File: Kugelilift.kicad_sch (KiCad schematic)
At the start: 16 parts, among them J2 TTL, J4 Stepper, SW1 RESET, SW2 MODE, SW3 SW_Push, SW4 SW_DIP_x04, U1 magnetic-charger, U2 TCRT5000, U3 ULN2003A, U5 UA78M33_TO252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

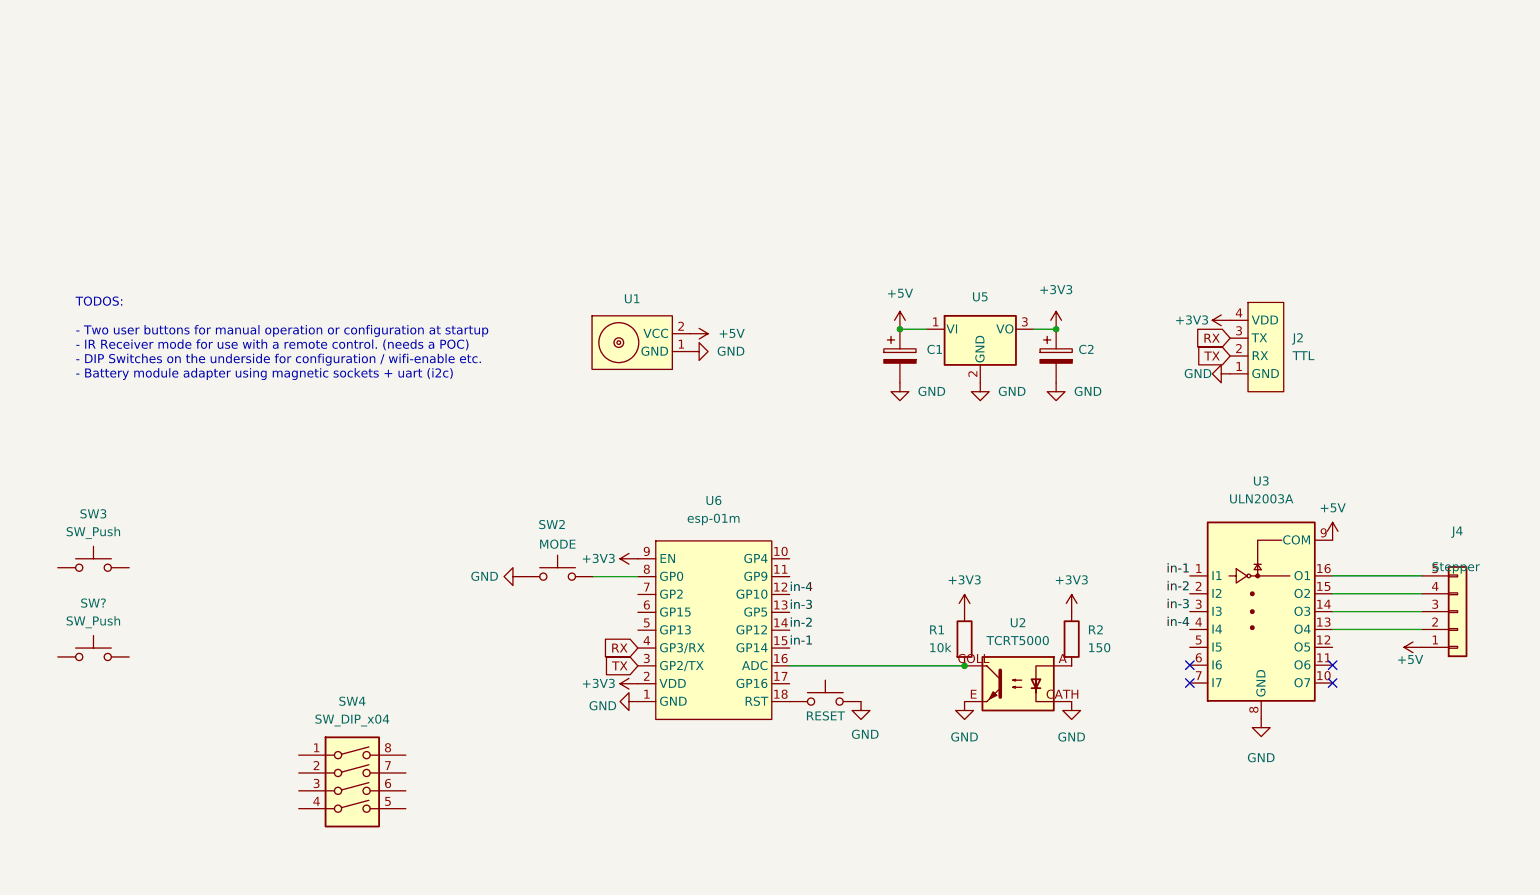
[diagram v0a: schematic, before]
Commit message: Laid out pushbuttons and dip switches
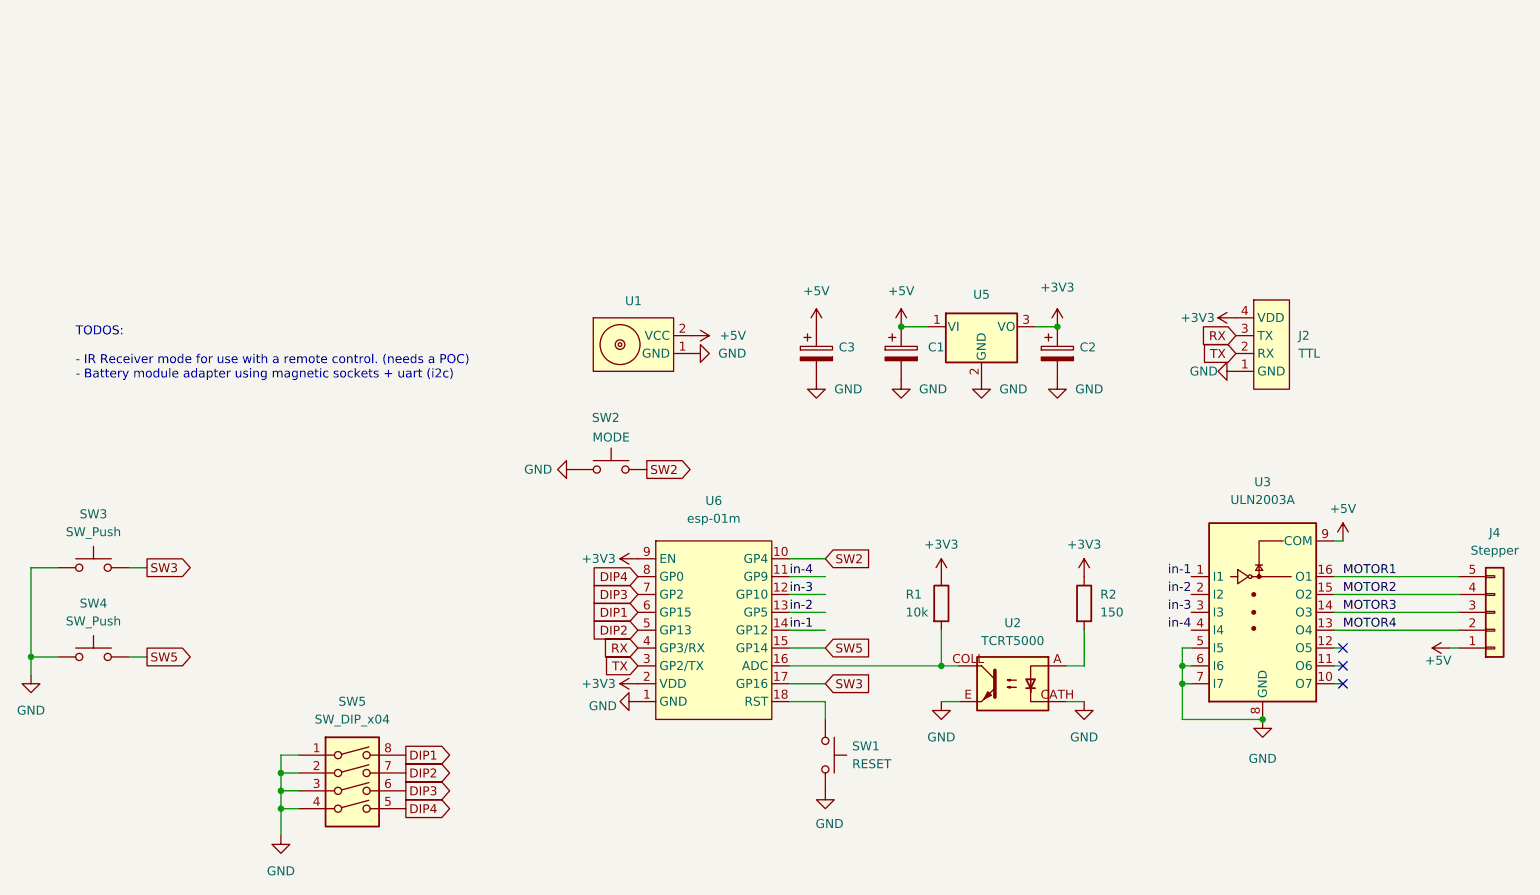
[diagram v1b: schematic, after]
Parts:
- added C3: C_Polarized, Capacitor_THT:CP_Radial_D6.3mm_P2.50mm, symbol Device:C_Polarized
- U3: footprint Package_SO:SOP-16_4.55x10.3mm_P1.27mm -> Package_SO:SOIC-16_3.9x9.9mm_P1.27mm
- gave numbers to parts that had none: 1
- renumbered SW4 to SW5
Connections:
- net +5V: now also C3.1
- net GND: now also SW3.1, SW4.1, SW5.1, SW5.2, SW5.3, SW5.4, U3.5 (I5), U3.6 (I6), U3.7 (I7), C3.2
- net in-1: now also U6.14 (GP12); no longer U6.15 (GP14)
- net in-2: now also U6.13 (GP5); no longer U6.14 (GP12)
- net in-3: now also U6.12 (GP10); no longer U6.13 (GP5)
- net in-4: now also U6.11 (GP9); no longer U6.12 (GP10)
- net MOTOR4: now reaches J4.2 (Pin_2), U3.13 (O4)
- net MOTOR3: now reaches J4.3 (Pin_3), U3.14 (O3)
- net MOTOR2: now reaches J4.4 (Pin_4), U3.15 (O2)
- net MOTOR1: now reaches J4.5 (Pin_5), U3.16 (O1)
- net DIP4: now reaches U6.8 (GP0)
- net DIP4: now also SW5.5; no longer SW2.1
- net SW2: now reaches U6.10 (GP4)
- net SW2: now also SW2.1
- net SW3: now reaches U6.17 (GP16)
- net SW3: now also SW3.2
- net DIP2: now reaches U6.5 (GP13)
- net DIP2: now also SW5.7
- net DIP1: now reaches U6.6 (GP15)
- net DIP1: now also SW5.8
- net DIP3: now reaches U6.7 (GP2)
- net DIP3: now also SW5.6
- net SW5: now reaches SW4.2
- net SW5: now also U6.15 (GP14)
- no-connect marks 4 -> 3
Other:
- note added: "TODOS: - IR Receiver mode for use with a remote control. (needs a POC) - Battery module adapter using magnetic sockets + uart (i2c)"
- note removed: "TODOS: - Two user buttons for manual operation or configuration at startup - IR Receiver mode for use with a remote control. (needs a POC) - DIP Switches on the underside for configuration / wifi-enable etc. - Battery module adapter using magnetic sockets + uart (i2c)"
- moved on the sheet: J2, J4, R1, R2, SW2, U2

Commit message: Update to "hard" pushbuttons, rearrange components.
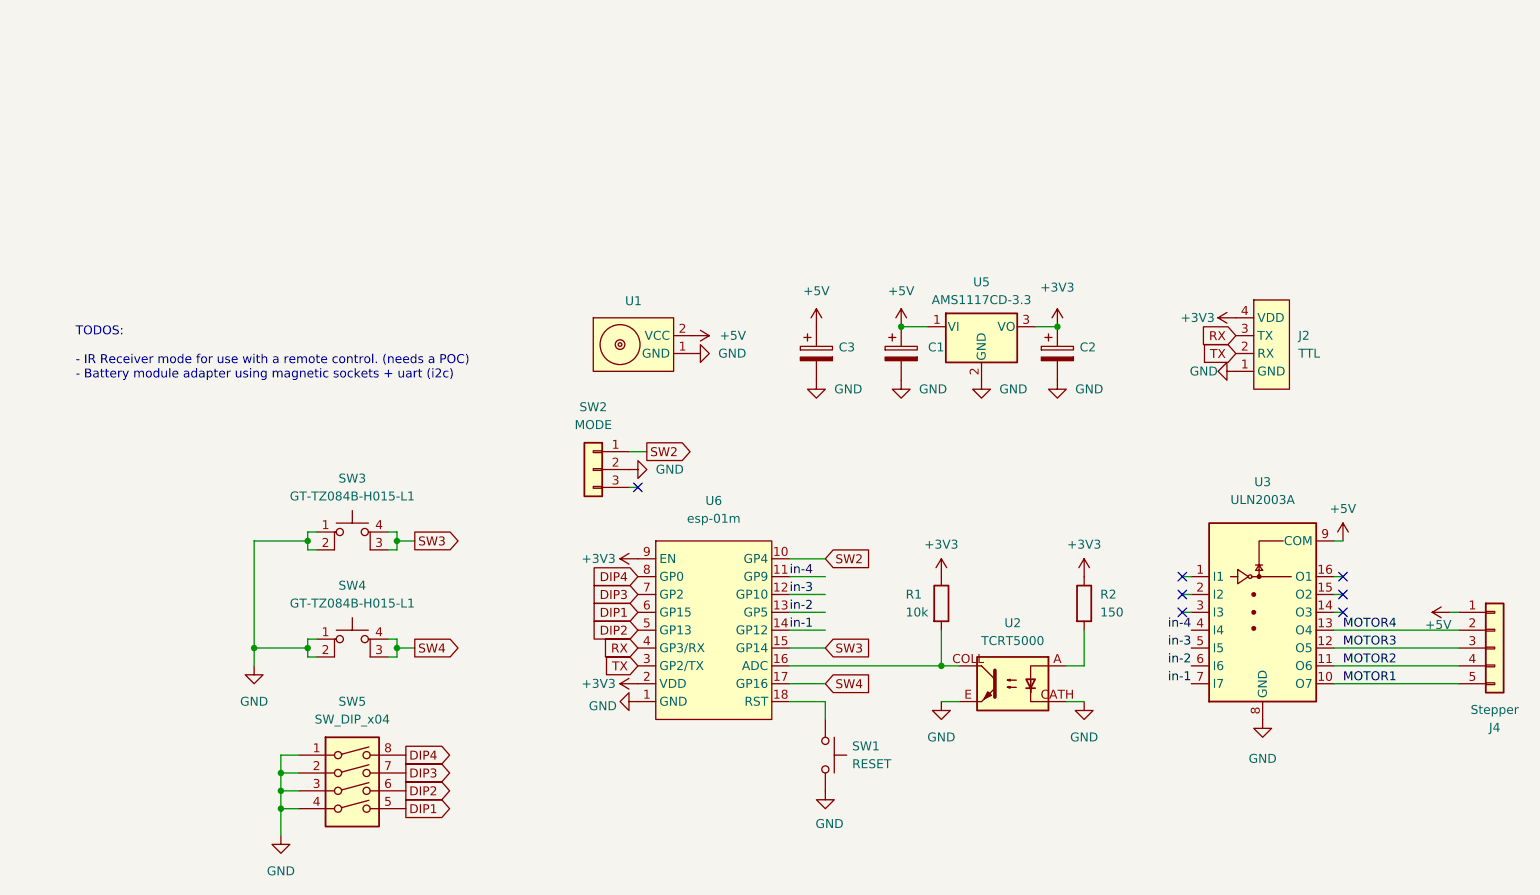
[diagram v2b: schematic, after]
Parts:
- removed SW3, SW4: SW_Push, Button_Switch_SMD:SW_Push_1P1T_NO_CK_KMR2, symbol Switch:SW_Push
- added SW3, SW4: GT-TZ084B-H015-L1, jlc_footprints:SW-SMD_4P-L5.2-W5.2-P3.70-LS6.4, symbol jlc_symbols:GT-TZ084B-H015-L1
- SW2: symbol Switch:SW_Push -> Connector_Generic:Conn_01x03
- U5: value UA78M33_TO252 -> AMS1117CD-3.3
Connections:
- net SW5 is gone; now on net SW3: U6.15 (GP14)
- net DIP1: now also SW5.5; no longer SW5.8
- net DIP2: now also SW5.6; no longer SW5.7
- net DIP3: now also SW5.7; no longer SW5.6
- net DIP4: now also SW5.8; no longer SW5.5
- net GND: now also SW3.1, SW3.2, SW4.1, SW4.2; no longer U3.5 (I5), U3.6 (I6), U3.7 (I7)
- net MOTOR1: now also U3.10 (O7); no longer U3.16 (O1)
- net MOTOR2: now also U3.11 (O6); no longer U3.15 (O2)
- net MOTOR3: now also U3.12 (O5); no longer U3.14 (O3)
- net SW3: now also SW3.3, SW3.4; no longer U6.17 (GP16)
- net in-1: now also U3.7 (I7); no longer U3.1 (I1)
- net in-2: now also U3.6 (I6); no longer U3.2 (I2)
- net in-3: now also U3.5 (I5); no longer U3.3 (I3)
- new net SW4: SW4.3, SW4.4, U6.17 (GP16)
- no-connect marks 3 -> 7
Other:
- moved on the sheet: J4

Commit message: Rearrange components.
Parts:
- added SW32: GT-TZ084B-H015-L1, jlc_footprints:SW-SMD_4P-L5.2-W5.2-P3.70-LS6.4, symbol jlc_symbols:GT-TZ084B-H015-L1
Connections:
- net GND: now also SW32.1, SW32.2
- net MOTOR1: now also U3.13 (O4); no longer U3.10 (O7)
- net MOTOR2: now also U3.14 (O3); no longer U3.11 (O6)
- net MOTOR3: now also U3.15 (O2); no longer U3.12 (O5)
- net MOTOR4: now also U3.16 (O1); no longer U3.13 (O4)
- net SW3: now also SW32.3, SW32.4
- net SW4: no longer SW4.4
- net in-1: now also U3.4 (I4); no longer U3.7 (I7)
- net in-2: now also U3.3 (I3); no longer U3.6 (I6)
- net in-3: now also U3.2 (I2); no longer U3.5 (I5)
- net in-4: now also U3.1 (I1); no longer U3.4 (I4)
- no-connect marks 7 -> 8
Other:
- moved on the sheet: J4, SW3

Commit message: Use the LED footprint.
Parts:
- added U4: SK6812MINI-E_C5149201, jlc_footprints:LED-SMD_L3.2-W2.8-LS5.9_SK6812MINI-E BACK, symbol jlc_symbols:SK6812MINI-E_C5149201
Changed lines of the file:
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@@
+	)
+	(symbol
+		(lib_id "jlc_symbols:SK6812MINI-E_C5149201")
+		(at 73.66 52.07 0)
+		(unit 1)
+		(exclude_from_sim no)
+		(in_bom yes)
+		(on_board yes)
+		(dnp no)
+		(fields_autoplaced yes)
+		(property "Reference" "U4"
+			(at 73.66 43.18 0)
+			(effects
+				(font
+					(size 1.27 1.27)
+				)
+			)
+		)
+		(property "Value" "SK6812MINI-E_C5149201"
+			(at 73.66 45.72 0)
+			(effects
+				(font
+					(size 1.27 1.27)
+				)
+			)
+		)
+		(property "Footprint" "jlc_footprints:LED-SMD_L3.2-W2.8-LS5.9_SK6812MINI-E BACK"
+			(at 73.66 62.23 0)
+			(effects
+				(font
+					(size 1.27 1.27)
+					(italic yes)
+				)
+				(hide yes)
+			)
+		)
+		(property "Datasheet" "https://atta.szlcsc.com/upload/public/pdf/source/20241205/F2A5A00C3A41F444A29929735E36DD04.pdf"
+			(at 71.374 51.943 0)
+			(effects
+				(font
+					(size 1.27 1.27)
+				)
+				(justify left)
+				(hide yes)
+			)
+		)
+		(property "Description" ""
+			(at 73.66 52.07 0)
+			(effects
+				(font
+					(size 1.27 1.27)
+				)
+				(hide yes)
+			)
+		)
+		(property "LCSC" "C5149201"
+			(at 73.66 52.07 0)
+			(effects
+				(font
+					(size 1.27 1.27)
+				)
+				(hide yes)
+			)
+		)
+		(pin "2"
+		)
+		(pin "1"
+		)
+		(pin "3"
+		)
+		(pin "4"
+		)
+		(instances
+			(project ""
+				(path "/6d69e3e0-eef7-4f7c-a0d6-a7389b974fcc"
+					(reference "U4")
+					(unit 1)
+				)
+			)
+		)
 	)
 	(symbol
